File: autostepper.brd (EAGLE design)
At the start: 50.2 x 43.2 mm, 26 parts, among them U1 V_REG_317SMD, Y2 SFE_COM-00094

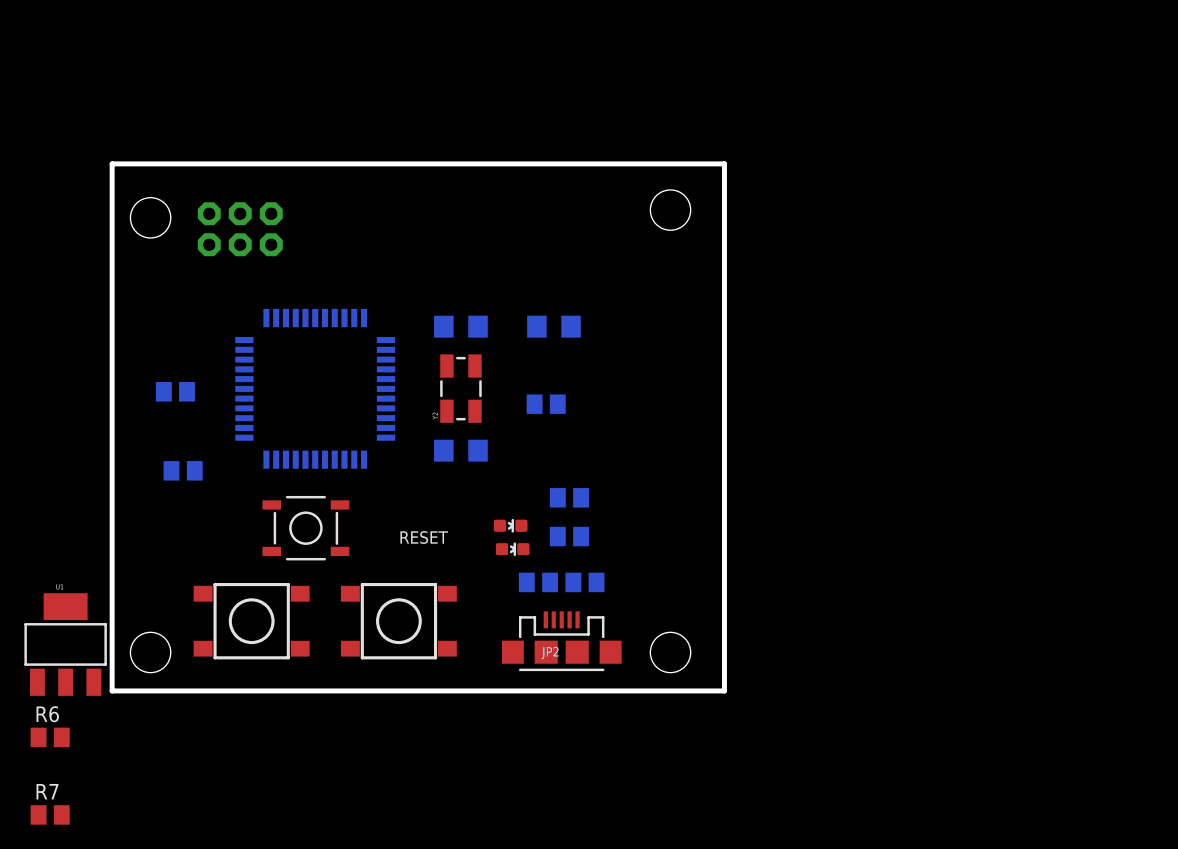
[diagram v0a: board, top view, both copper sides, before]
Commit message: Connectors added
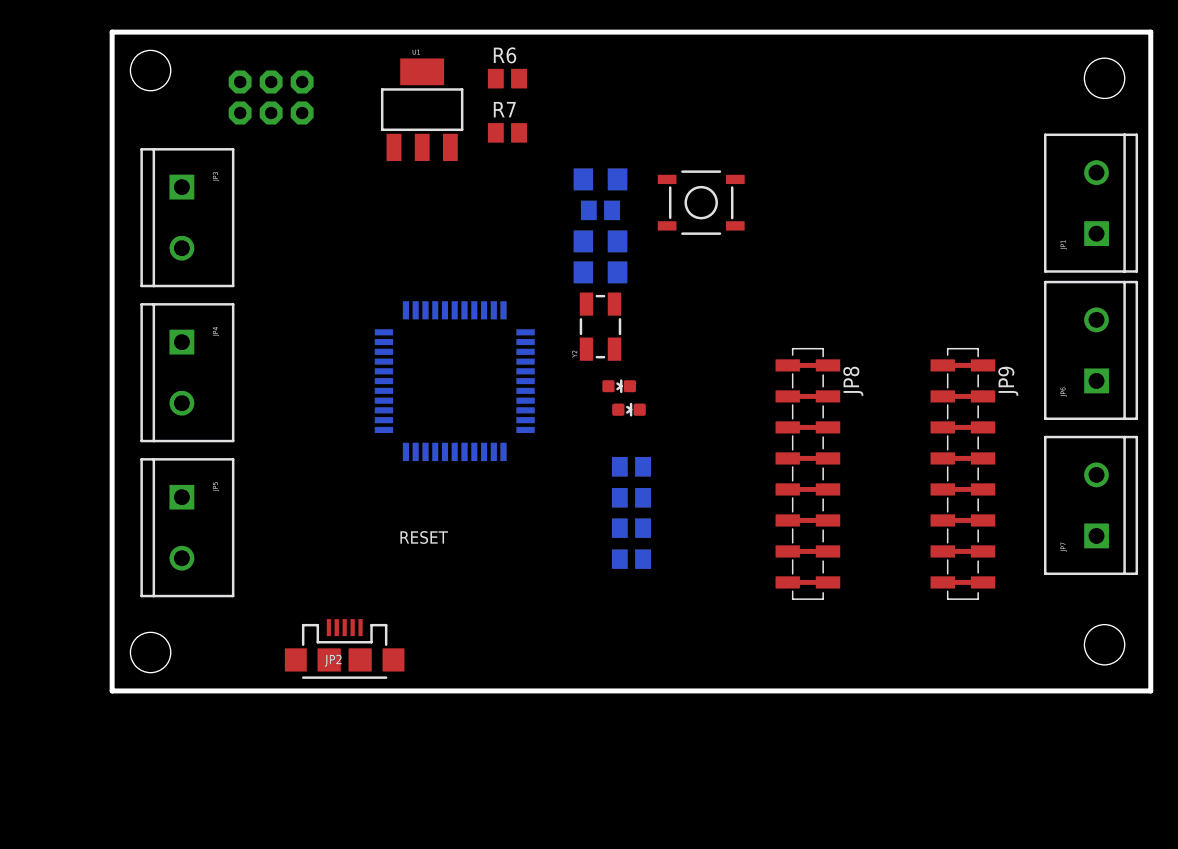
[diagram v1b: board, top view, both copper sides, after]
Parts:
- removed R4, R5: 10k, rcl:M0805
- removed S2: DOWN, SparkFun-Electromechanical:TACTILE_SWITCH_TALL
- removed S9: UP, SparkFun-Electromechanical:TACTILE_SWITCH_TALL
- added JP1: VMOT, SparkFun-Connectors:SCREWTERMINAL-5MM-2
- added JP3: BTN_A, SparkFun-Connectors:SCREWTERMINAL-5MM-2
- added JP4: BTN_B, SparkFun-Connectors:SCREWTERMINAL-5MM-2
- added JP5: BTN_C, SparkFun-Connectors:SCREWTERMINAL-5MM-2
- added JP6: COIL_A, SparkFun-Connectors:SCREWTERMINAL-5MM-2
- added JP7: COIL_B, SparkFun-Connectors:SCREWTERMINAL-5MM-2
- added JP8, JP9: (no value), SparkFun-Connectors:1X08_SMD_COMBINED
- moved R7 67.3 mm to (32.4, 45.7)
- moved R6 65.7 mm to (32.4, 50.2)
- moved U1 52.7 mm to (25.4, 47.6)
- moved S1 42.0 mm to (48.3, 40.0)
- moved U$6 37.2 mm to (81.3, 50.2)
- moved U$5 35.6 mm to (81.3, 3.78)
- moved C3 20.6 mm to (40.0, 36.8)
- moved JP2 17.8 mm to (19.1, 2.54)
- moved R1 16.5 mm to (40.0, 39.4)
- moved LED3 14.9 mm to (42.3, 23.0)
- moved LED2 14.5 mm to (41.5, 25.0)
- moved C1 12.7 mm to (40.0, 41.9)
- moved Y2 12.5 mm to (40.0, 29.8)
- moved C2 12.3 mm to (40.0, 34.3)
- moved U$2 12.1 mm to (3.15, 50.8)
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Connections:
- removed net DOWN: R5.2, S2.B2
- removed net UP: R4.2, S9.B2
- new net A4988_1A: JP9.4
- new net A4988_1B: JP9.3
- new net A4988_2A: JP9.5
- new net A4988_2B: JP9.6
- new net A4988_DIR: JP8.1
- new net A4988_ENABLE: JP8.8
- new net A4988_GND: JP9.1, JP9.7
- new net A4988_MS1: JP8.7
- new net A4988_MS2: JP8.6
- new net A4988_MS3: JP8.5
- new net A4988_RESET: JP8.4
- new net A4988_SLEEP: JP8.3
- new net A4988_STEP: JP8.2
- new net A4988_VDD: JP9.2
- new net A4988_VMOT: JP9.8
- net 3.3V: no longer S2.A2, S9.A2
- net GND: now also JP1.2, JP3.2, JP4.2, JP5.2; no longer R4.1, R5.1
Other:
- board size 50.2 x 43.2 mm -> 85.1 x 54 mm

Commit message: Layout fix
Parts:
- removed JP3: BTN_A, SparkFun-Connectors:SCREWTERMINAL-5MM-2
- removed JP4: BTN_B, SparkFun-Connectors:SCREWTERMINAL-5MM-2
- removed JP5: BTN_C, SparkFun-Connectors:SCREWTERMINAL-5MM-2
- added C4: 47uF, SparkFun-Passives:PANASONIC_D
- added C5: 1uF, SparkFun-Passives:1206
- added C6: .1uF, SparkFun-Passives:1206
- added D1: B340A-13-F, SparkFun-DiscreteSemi:DIODE-HV
- added J1: (no value), SparkFun-Connectors:1X04_LONGPADS
- JP8, JP9: device SparkFun-Connectors:1X08_SMD_COMBINED -> SparkFun-Connectors:1X08_LONGPADS
- moved LED3 44.9 mm to (2.34, 43.4)
- moved C1 44.4 mm to (17.1, 3.81)
- moved LED2 43.7 mm to (2.80, 45.3)
- moved R1 40.5 mm to (16.5, 6.35)
- moved JP1 37.6 mm to (45.1, 49.5), turned to 180 degrees
- moved C2 34.1 mm to (16.5, 9.53)
- moved S1 33.7 mm to (14.6, 39.4)
- moved C3 33.2 mm to (17.1, 12.7)
- moved R13 31.9 mm to (11.4, 8.84)
- moved R14 31.9 mm to (11.4, 11.4)
- moved R2 31.9 mm to (11.4, 6.35)
- moved R3 31.9 mm to (11.4, 3.81)
- moved U$5 24.1 mm to (57.2, 3.78)
- moved U$6 23.5 mm to (57.8, 50.8)
- moved JP9 21.4 mm to (48.9, 21.7), turned to 180 degrees
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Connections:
- removed net N$3: R6.2, U1.2
- new net BUTTON_A: J1.1, U$1.25
- new net BUTTON_B: J1.2, U$1.31
- new net BUTTON_C: J1.3, U$1.27
- new net N$8: C4.+, C6.1, D1.C, U1.3
- net 3.3V: now also C5.1, R14.1, R6.2, U1.2
- net A4988_1A: now also JP6.2, JP7.1
- net A4988_1B: now also JP7.2
- net A4988_2A: now also JP6.1
- net A4988_VMOT: now also D1.A, JP1.1
- net GND: now also C4.-, C5.2, C6.2, J1.4; no longer JP3.2, JP4.2, JP5.2
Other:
- board size 85.1 x 54 mm -> 79.4 x 54 mm
- board text removed: "RESET"
